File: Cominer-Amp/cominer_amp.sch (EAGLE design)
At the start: 69 parts, among them IC1 OP-AMP, J2 AVR_SPI_PROG_5X2LOCK, J3 AUDIO_JACK_3.5MM_PTH, J4 AUDIO_JACK_3.5MM_PTH, J5 AUDIO_JACK_3.5MM_PTH, J6 AUDIO_JACK_3.5MM_PTH, J7 MOLEX-CPU-POWER, J8 POWER_JACKSLT, Q1 220mA/50V/3.5Ω, Q2 220mA/50V/3.5Ω, Q3 220mA/50V/3.5Ω, Q4 220mA/50V/3.5Ω, Q5 220mA/50V/3.5Ω, Q6 220mA/50V/3.5Ω, Q7 20V/2A, U1 ESP-07, U2 ATMEGA16U2, U3 LM1117-3.3v, U4 LM1117-5v, U5 ADS1015, U6 ADS1015, Y1 16MHz

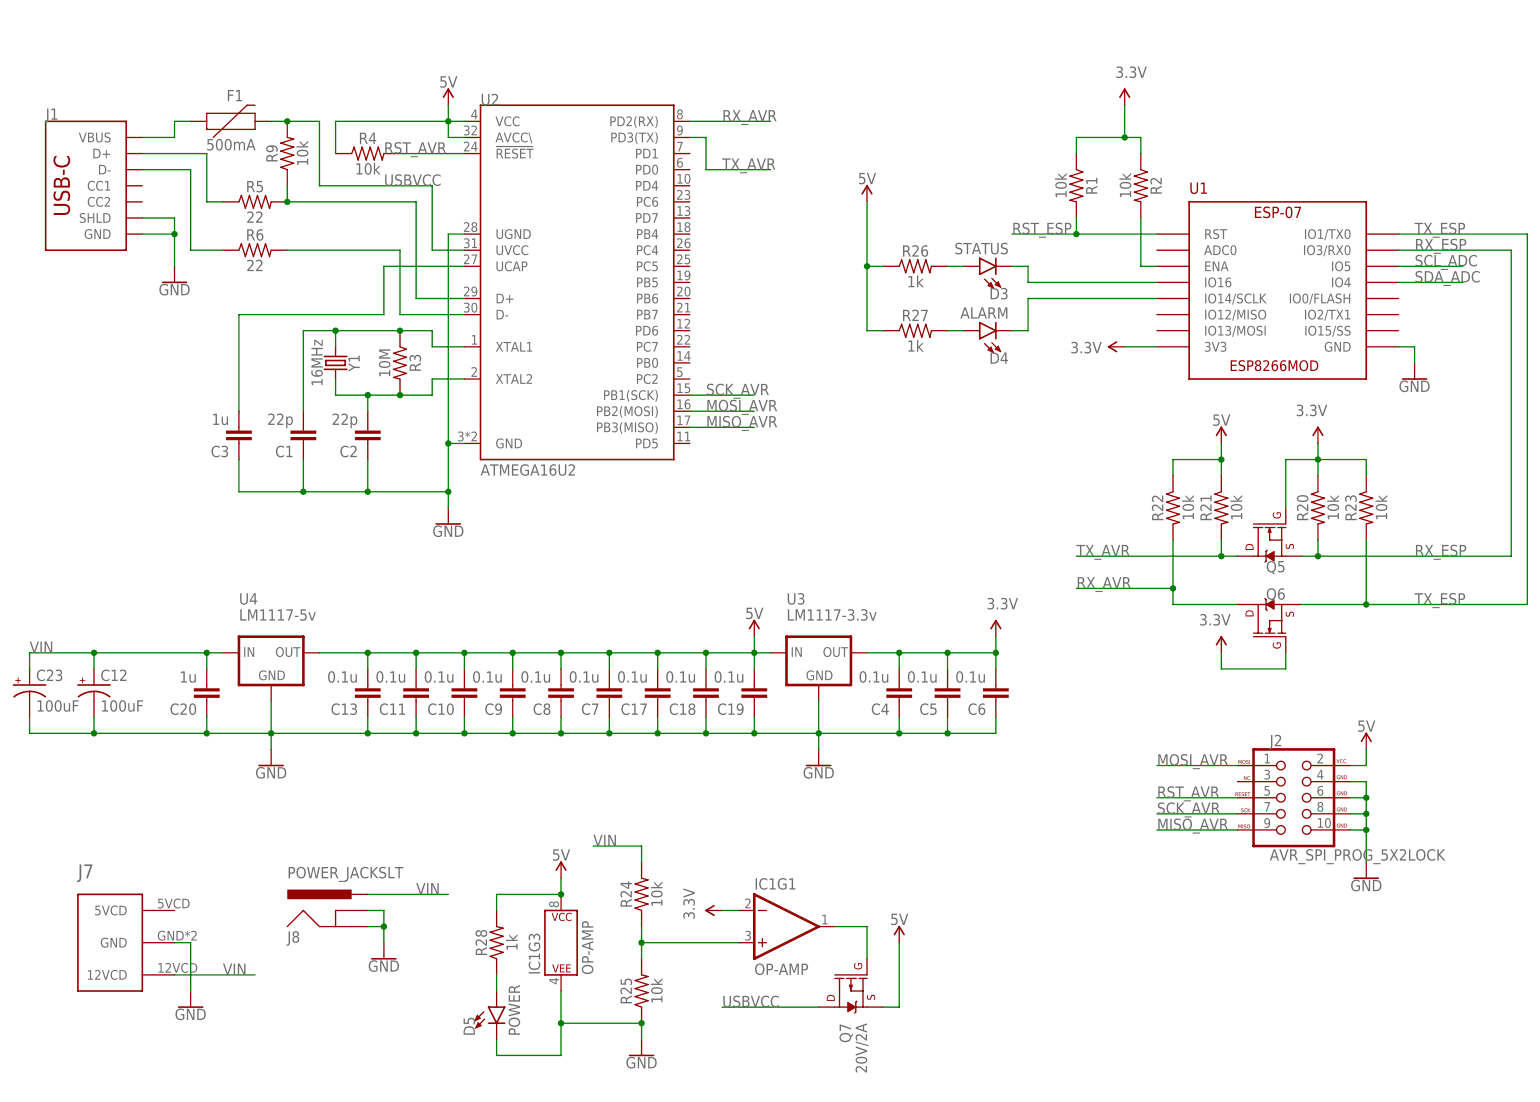
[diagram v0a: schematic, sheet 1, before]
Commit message: add serial and amp board
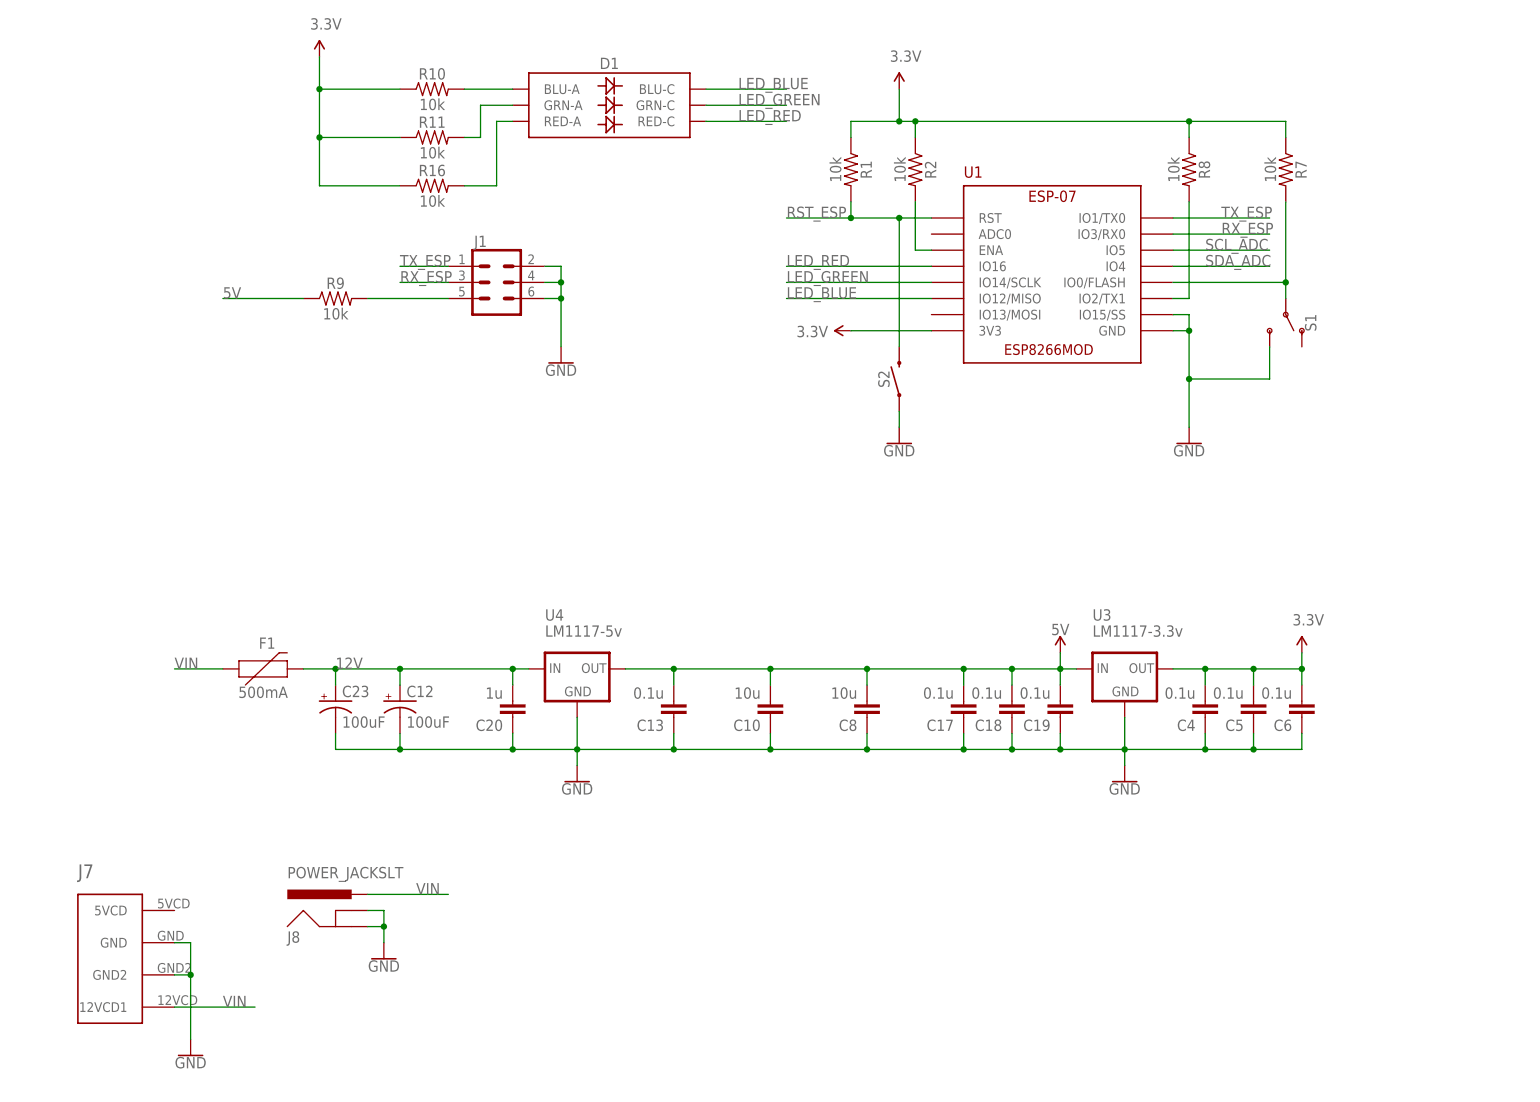
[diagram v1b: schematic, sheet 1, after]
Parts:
- removed C1, C2: 22p, SparkFun-Capacitors:CAP-0805
- removed C11, C7, C9: 0.1u, SparkFun-Capacitors:CAP-0805
- removed C3: 1u, SparkFun-Capacitors:CAP-0805
- removed D3: STATUS, SparkFun-LED:LED-YELLOW0603
- removed D4: ALARM, SparkFun-LED:LED-YELLOW0603
- removed D5: POWER, SparkFun-LED:LED-YELLOW0603
- removed IC1: OP-AMP, SparkFun-IC-Amplifiers:OPAMP-DUALU
- removed J2: AVR_SPI_PROG_5X2LOCK, SparkFun-Connectors:AVR_SPI_PROG_5X2LOCK
- removed Q3, Q4, Q5, Q6: 220mA/50V/3.5Ω, SparkFun-DiscreteSemi:MOSFET-NCH-BSS138
- removed Q7: 20V/2A, SparkFun-DiscreteSemi:MOSFET_PCH-DMG2305UX-7
- removed R17, R18, R19, R20, R21, R22, R23, R24, R25: 10k, SparkFun-Resistors:RESISTOR0805
- removed R26, R27, R28: 1k, SparkFun-Resistors:RESISTOR0805
- removed U2: ATMEGA16U2, Cominer-Microcontroller:ATMEGA16U2
- removed Y1: 16MHz, SparkFun-Clocks:CRYSTAL-16MHZSMD-5X3.2
- added D1: (no value), SparkFun-LED:LED-RGBNO_IC
- added R10, R11, R7, R8: 10k, SparkFun-Resistors:RESISTOR0805
- added S1: (no value), SparkFun-Switches:SWITCH-SPDT-SMD-RIGHT-ANGLE
- added S2: MOMENTARY-SWITCH-SPST-SMD-6.0X3.5MM, SparkFun-Switches:MOMENTARY-SWITCH-SPST-SMD-6.0X3.5MM
- C10, C8: value 0.1u -> 10u
- J1: device SparkFun-Connectors:USB_C_2-LAYER_PADS -> SparkFun-Connectors:CONN_03X2SHROUD
- J7: device Cominer-Connectors:MOLEX-CPU-POWER -> MolexConn:MOLEX-CPU-POWER
- Q1, Q2: value 220mA/50V/3.5Ω -> BSS138
- R3: value 10M -> 33
- R4: value 10k -> 33
- R5, R6: value 22 -> 33
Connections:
- removed net MISO_AVR: J2.MISO, U2.PB3(MISO)
- removed net MOSI_AVR: J2.MOSI, U2.PB2(MOSI)
- removed net N$18: J4.TIP, U5.AIN3
- removed net N$26: Q3.D, R17.2, U6.SCL
- removed net N$27: Q4.D, R18.2, U6.SDA
- removed net N$28: IC1G1.OUT, Q7.G
- removed net N$29: IC1G1.+IN, R24.1, R25.2
- removed net N$30: D3.C, U1.IO16
- removed net N$31: D4.C, U1.IO14/SCLK
- removed net N$32: D3.A, R26.2
- removed net N$33: D4.A, R27.2
- removed net N$36: D5.A, R28.1
- removed net N$6: R6.2, U2.D-
- removed net N$7: R5.2, R9.1, U2.D+
- removed net RST_AVR: J2.RESET, R4.2, U2.!RESET
- removed net RX_AVR: Q6.D, R22.2, U2.PD2(RX)
- removed net SCK_AVR: J2.SCK, U2.PB1(SCK)
- removed net TX_AVR: Q5.D, R21.2, U2.PD3(TX)
- removed net USBVCC: F1.2, Q7.D, R9.2, U2.UVCC
- new net 12V: C12.+, C20.2, C23.+, F1.2, U4.IN
- new net LED_BLUE: D1.BLU-C, U1.IO12/MISO
- new net LED_GREEN: D1.GRN-C, U1.IO14/SCLK
- new net LED_RED: D1.RED-C, U1.IO16
- new net N$4: J1.5, R9.2
- net 3.3V: now also R10.1, R11.1, R7.1, R8.1; no longer IC1G1.-IN, Q3.G, Q4.G, Q5.G, Q6.G, R19.1, R20.1, R23.1
- net 5V: now also R9.1; no longer C11.2, C7.2, C9.2, IC1G3.P$V+, J2.VCC, J3.TSH, J4.TSH, J5.TSH, J6.TSH, Q7.S, R17.1, R18.1, R21.1, R22.1, R26.1, R27.1, R28.2, R4.1, U2.AVCC\, U2.VCC
- net GND: now also J1.2, J1.4, J1.6, J7.GND2, S1.S, S2.1, U1.IO15/SS; no longer C1.1, C11.1, C2.1, C3.1, C7.1, C9.1, D5.C, IC1G3.P$V-, J1.GND, J1.SHLD, J2.GND@1, J2.GND@2, J2.GND@3, J2.GND@4, R25.1, U2.GND, U2.UGND
- net N$1: now also J4.TIP, R5.2, U5.AIN3; no longer C1.2, R3.1, U2.XTAL1, Y1.1
- net N$10: now also D1.RED-A, R16.2; no longer F1.1, J1.VBUS
- net N$16: now also R4.1
- net N$17: now also R4.2
- net N$19: now also R5.1
- net N$2: now also R7.2, S1.P, U1.IO0/FLASH; no longer C2.2, R3.2, U2.XTAL2, Y1.2
- net N$20: now also R3.2
- net N$21: now also U6.SDA
- net N$22: now also R3.1
- net N$23: now also U6.SCL
- net N$24: now also R6.2
- net N$25: now also R6.1
- net N$3: now also R8.2, U1.IO2/TX1; no longer C3.2, U2.UCAP
- net N$8: now also D1.BLU-A, R10.2; no longer J1.D+, R5.1
- net N$9: now also D1.GRN-A, R11.2; no longer J1.D-, R6.1
- net RST_ESP: now also S2.2
- net RX_ESP: now also J1.3; no longer Q5.S, R20.2
- net SCL_ADC: no longer Q3.S, R16.2
- net SDA_ADC: no longer Q4.S, R19.2
- net TX_ESP: now also J1.1; no longer Q6.S, R23.2
- net VIN: now also F1.1, J7.12VCD1; no longer C12.+, C20.2, C23.+, J7.12VCD, R24.2, U4.IN
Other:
- moved on the sheet: C10, C12, C13, C17, C18, C19, C20, C23, C4, C5, C6, C8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
